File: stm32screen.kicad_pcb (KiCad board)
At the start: 4 copper layers, 46 x 46 mm, 40 parts, among them J1 SWD, J2 GC9A01, J3 OIL, J4 PRESS, J5 POWER IN, J6 EGT, SW1 NRST, SW2 USER, U1 TS1117BCW-3.3, U2 STM32F407VETx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

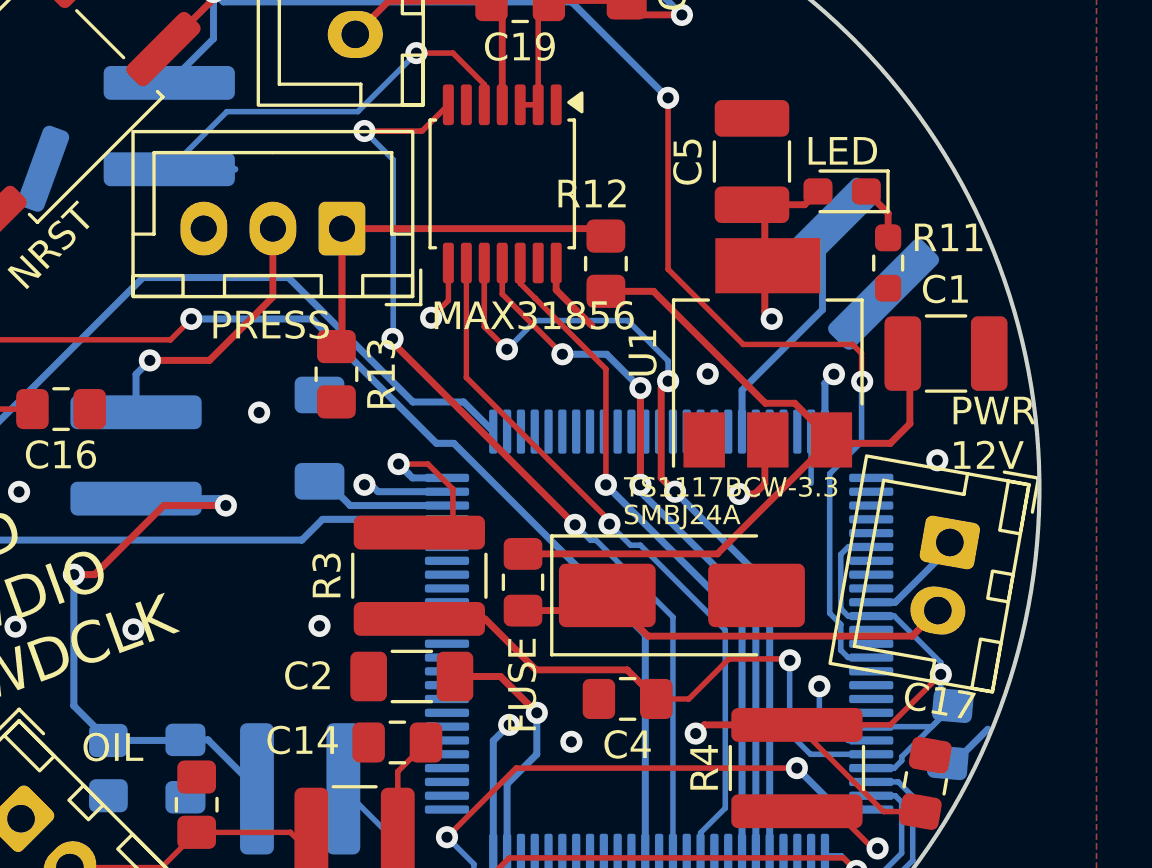
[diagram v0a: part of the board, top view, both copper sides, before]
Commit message: Ground pour spacing 0.2mm, small trace fixes.
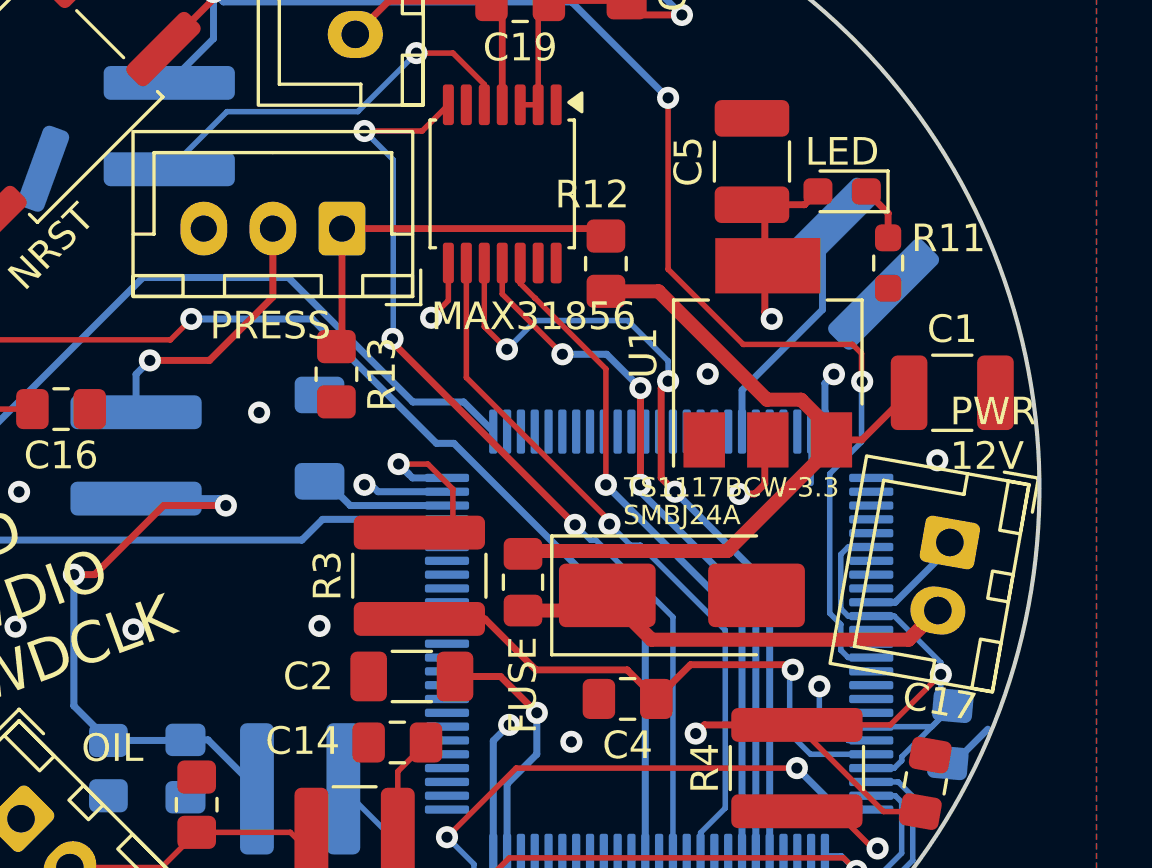
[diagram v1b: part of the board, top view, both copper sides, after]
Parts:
- moved C1 1.44 mm to (142.8, 68.2)
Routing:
- net GND: track 19.5 -> 16.7 mm
- net VDD: track 101.9 -> 99.5 mm
- net Vin: track 28.3 -> 27.3 mm
- net Net-(U2-VREF+): track 21.7 -> 21.0 mm
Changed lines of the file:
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@@
 			(pinfunction "A")
 			(pintype "passive")
+			(zone_connect 2)
 		)
 		(embedded_fonts no)
@@
 	(footprint "Capacitor_SMD:C_1210_3225Metric_Pad1.33x2.70mm_HandSolder"
 		(layer "F.Cu")
-		(at 142.5571 66.7512)
+		(at 142.7825 68.17)
 		(descr "Capacitor SMD 1210 (3225 Metric), square (rectangular) end terminal, IPC-7351 nominal with elongated pad for handsoldering. (Body size source: IPC-SM-782 page 76, https://www.pcb-3d.com/wordpress/wp-content/uploads/ipc-sm-782a_amendment_1_and_2.pdf), generated with kicad-footprint-generator")
 		(tags "capacitor handsolder")
@@
 			(pinfunction "DGND")
 			(pintype "power_in")
+			(zone_connect 2)
 		)
 		(embedded_fonts no)
@@
 	)
 	(segment
-		(start 134.2826 74)
-		(end 138.4072 69.8754)
-		(width 0.25)
+		(start 137.3122 68.4204)
+		(end 138.4072 69.5154)
+		(width 0.508)
 		(layer "F.Cu")
 		(net 1)
 	)
 	(segment
-		(start 138.3 70)
-		(end 140.5406 70)
-		(width 0.254)
+		(start 138.4072 69.8754)
+		(end 139.5146 69.8754)
+		(width 0.25)
 		(layer "F.Cu")
 		(net 1)
 	)
 	(segment
-		(start 130.25 64.5)
-		(end 131.97312 64.5)
+		(start 139.5146 69.8754)
+		(end 141.22 68.17)
 		(width 0.25)
 		(layer "F.Cu")
@@
 	)
 	(segment
-		(start 140.5406 70)
-		(end 141.2486 69.292)
-		(width 0.254)
+		(start 130.25 64.5)
+		(end 132.155553 64.5)
+		(width 0.508)
 		(layer "F.Cu")
 		(net 1)
 	)
 	(segment
-		(start 136.02252 68.5494)
-		(end 137.0812 68.5494)
-		(width 0.25)
+		(start 127.355 73.895)
+		(end 134.6376 73.895)
+		(width 0.508)
 		(layer "F.Cu")
 		(net 1)
 	)
 	(segment
-		(start 137.0812 68.5494)
-		(end 138.4072 69.8754)
-		(width 0.25)
+		(start 127.25 74)
+		(end 127.355 73.895)
+		(width 0.508)
 		(layer "F.Cu")
 		(net 1)
 	)
 	(segment
-		(start 131.97312 64.5)
-		(end 136.02252 68.5494)
-		(width 0.25)
+		(start 138.4072 69.5154)
+		(end 138.4072 69.8754)
+		(width 0.508)
 		(layer "F.Cu")
 		(net 1)
 	)
 	(segment
-		(start 138.3 69.8)
-		(end 138.3 70)
-		(width 0.254)
+		(start 136.075953 68.4204)
+		(end 137.3122 68.4204)
+		(width 0.508)
 		(layer "F.Cu")
 		(net 1)
 	)
 	(segment
-		(start 141.2486 69.292)
-		(end 141.2486 67.7164)
-		(width 0.254)
+		(start 132.155553 64.5)
+		(end 136.075953 68.4204)
+		(width 0.508)
 		(layer "F.Cu")
 		(net 1)
 	)
 	(segment
-		(start 127.25 74)
-		(end 134.2826 74)
-		(width 0.25)
+		(start 138.3 69.8)
+		(end 138.3 70)
+		(width 0.254)
 		(layer "F.Cu")
 		(net 1)
 	)
 	(segment
-		(start 128.45 63.475)
-		(end 128.45 64.45)
-		(width 0.25)
+		(start 138.4072 70.1254)
+		(end 138.4072 69.8754)
+		(width 0.508)
 		(layer "F.Cu")
-		(net 2)
+		(net 1)
 	)
 	(segment
-		(start 128.45 64.45)
-		(end 129.75 65.75)
-		(width 0.25)
+		(start 134.6376 73.895)
+		(end 138.4072 70.1254)
+		(width 0.508)
 		(layer "F.Cu")
-		(net 2)
+		(net 1)
 	)
 	(segment
@@
 	)
 	(segment
-		(start 114.4524 60.0841)
-		(end 116.8274 60.0841)
-		(width 0.25)
-		(layer "B.Cu")
-		(net 5)
-	)
-	(segment
 		(start 137.353 87.593636)
 		(end 137.353 88.3299)
@@
 	)
 	(segment
-		(start 133.25 79.25)
-		(end 134.7 77.8)
-		(width 0.2)
+		(start 131.0212 78.197)
+		(end 132.0722 79.248)
+		(width 0.25)
 		(layer "F.Cu")
 		(net 6)
 	)
 	(segment
-		(start 134.7 77.8)
-		(end 137.2 77.8)
-		(width 0.2)
+		(start 132.0722 79.248)
+		(end 133.3102 78.01)
+		(width 0.25)
 		(layer "F.Cu")
 		(net 6)
 	)
 	(segment
-		(start 131.0212 78.197)
-		(end 132.0722 79.248)
+		(start 133.3102 78.01)
+		(end 136.83 78.01)
 		(width 0.25)
 		(layer "F.Cu")
@@
 	)
 	(segment
-		(start 123.5 76.3532)
-		(end 125.875 76.3532)
+		(start 136.83 78.01)
+		(end 137.01 78.19)
 		(width 0.25)
 		(layer "F.Cu")
@@
 	)
 	(segment
-		(start 132 79.25)
-		(end 133.25 79.25)
-		(width 0.2)
+		(start 123.5 76.3532)
+		(end 125.875 76.3532)
+		(width 0.25)
 		(layer "F.Cu")
 		(net 6)
@@
 	)
 	(via
-		(at 136.906 77.851)
+		(at 137.01 78.19)
 		(size 0.8)
 		(drill 0.4)
@@
 	)
 	(segment
-		(start 136.899 78.101)
-		(end 137.2 77.8)
-		(width 0.2)
-		(layer "B.Cu")
-		(net 6)
-	)
-	(segment
 		(start 114.25 72.25)
 		(end 116.5 72.25)
@@
 	)
 	(segment
-		(start 131.776 76.976)
-		(end 130.3 75.5)
-		(width 0.25)
+		(start 141.204538 77.105)
+		(end 142.260563 76.048975)
+		(width 0.508)
 		(layer "F.Cu")
 		(net 10)
@@
 		(start 129.75 76.05)
 		(end 130.3 75.5)
-		(width 0.25)
+		(width 0.508)
 		(layer "F.Cu")
 		(net 10)
 	)
 	(segment
-		(start 142.260563 76.048975)
-		(end 141.333538 76.976)
-		(width 0.25)
+		(start 131.905 77.105)
+		(end 141.204538 77.105)
+		(width 0.508)
 		(layer "F.Cu")
 		(net 10)
 	)
 	(segment
-		(start 127.25 76.05)
-		(end 129.75 76.05)
-		(width 0.25)
+		(start 130.3 75.5)
+		(end 131.905 77.105)
+		(width 0.508)
 		(layer "F.Cu")
 		(net 10)
 	)
 	(segment
-		(start 141.333538 76.976)
-		(end 131.776 76.976)
-		(width 0.25)
+		(start 127.25 76.05)
+		(end 129.75 76.05)
+		(width 0.508)
 		(layer "F.Cu")
 		(net 10)
@@
 		(layers "F.Cu" "B.Cu" "In2.Cu")
 		(hatch edge 0.5)
-		(connect_pads
-			(clearance 0.508)
+		(connect_pads thru_hole_only
+			(clearance 0.2)
 		)
 		(min_thickness 0.25)
